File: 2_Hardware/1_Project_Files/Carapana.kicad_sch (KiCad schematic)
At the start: 0 parts

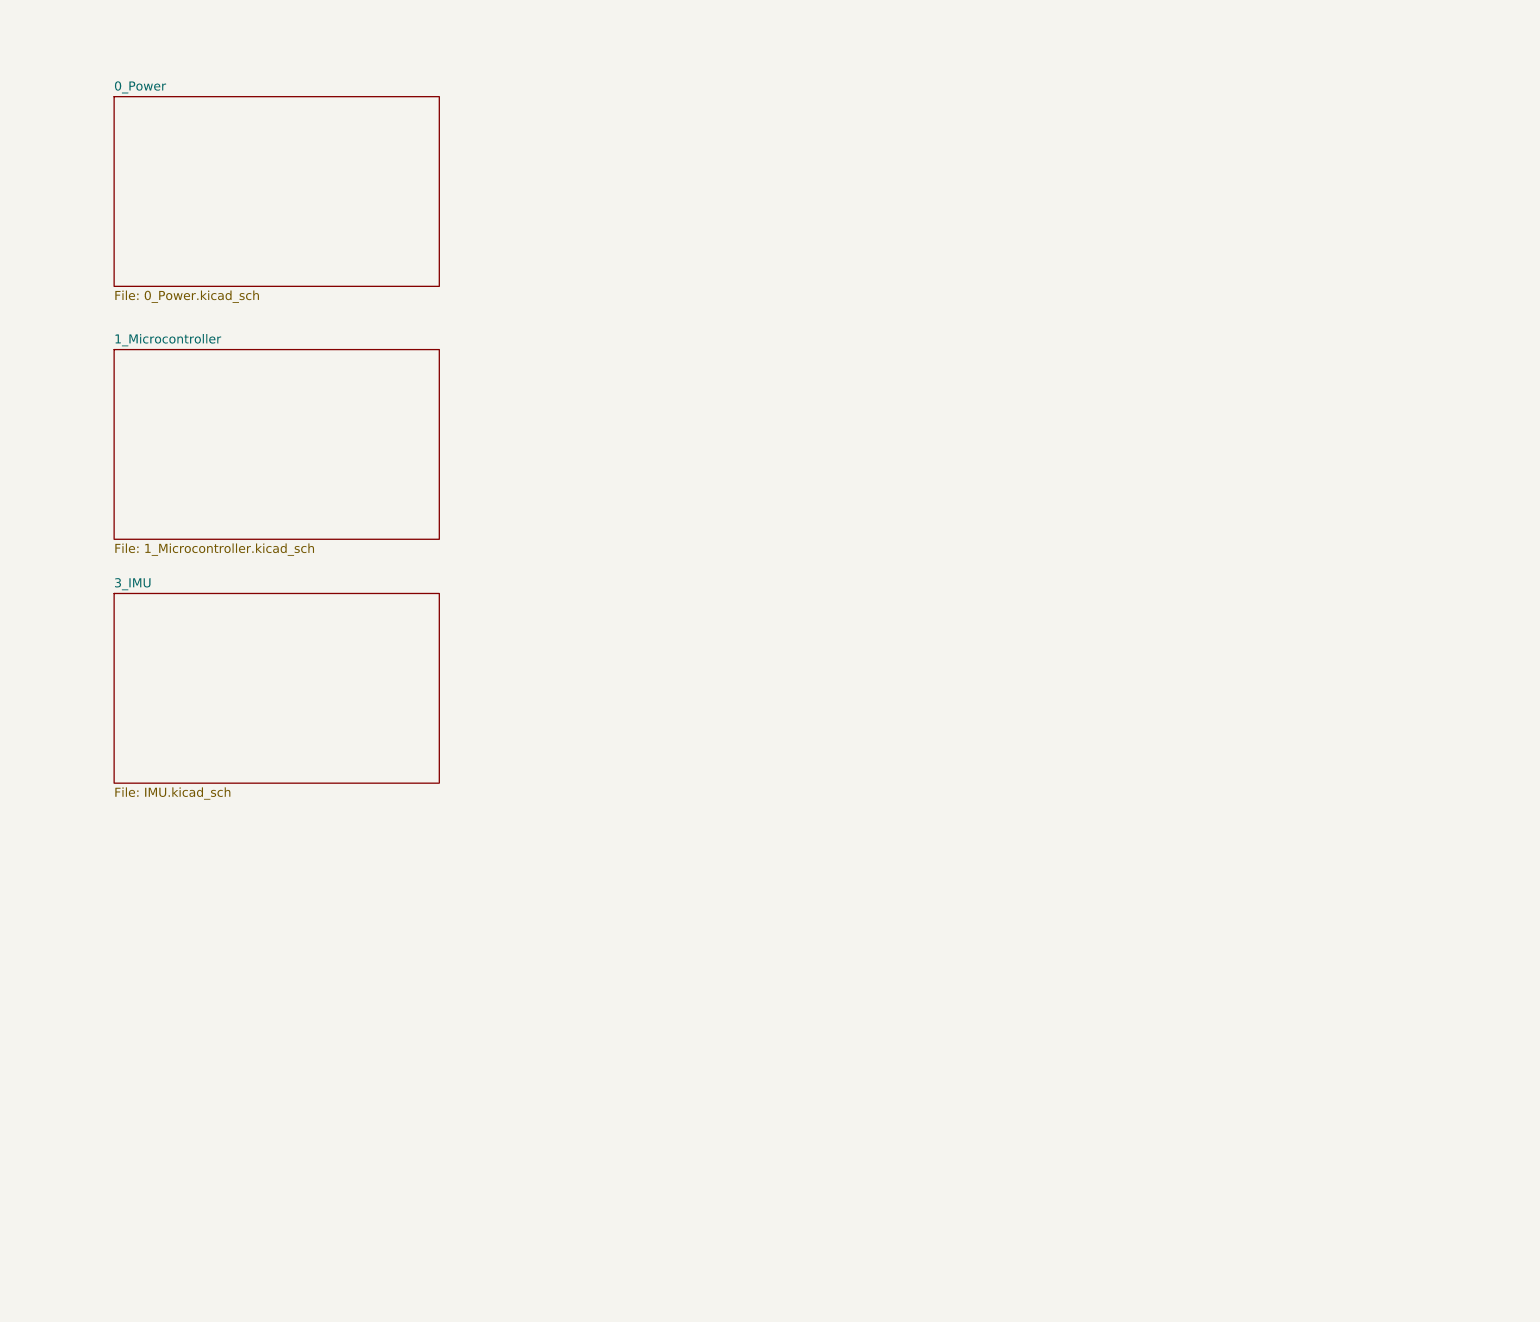
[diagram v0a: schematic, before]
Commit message: Adds 2_Motors schematic sheet and updates block diagram
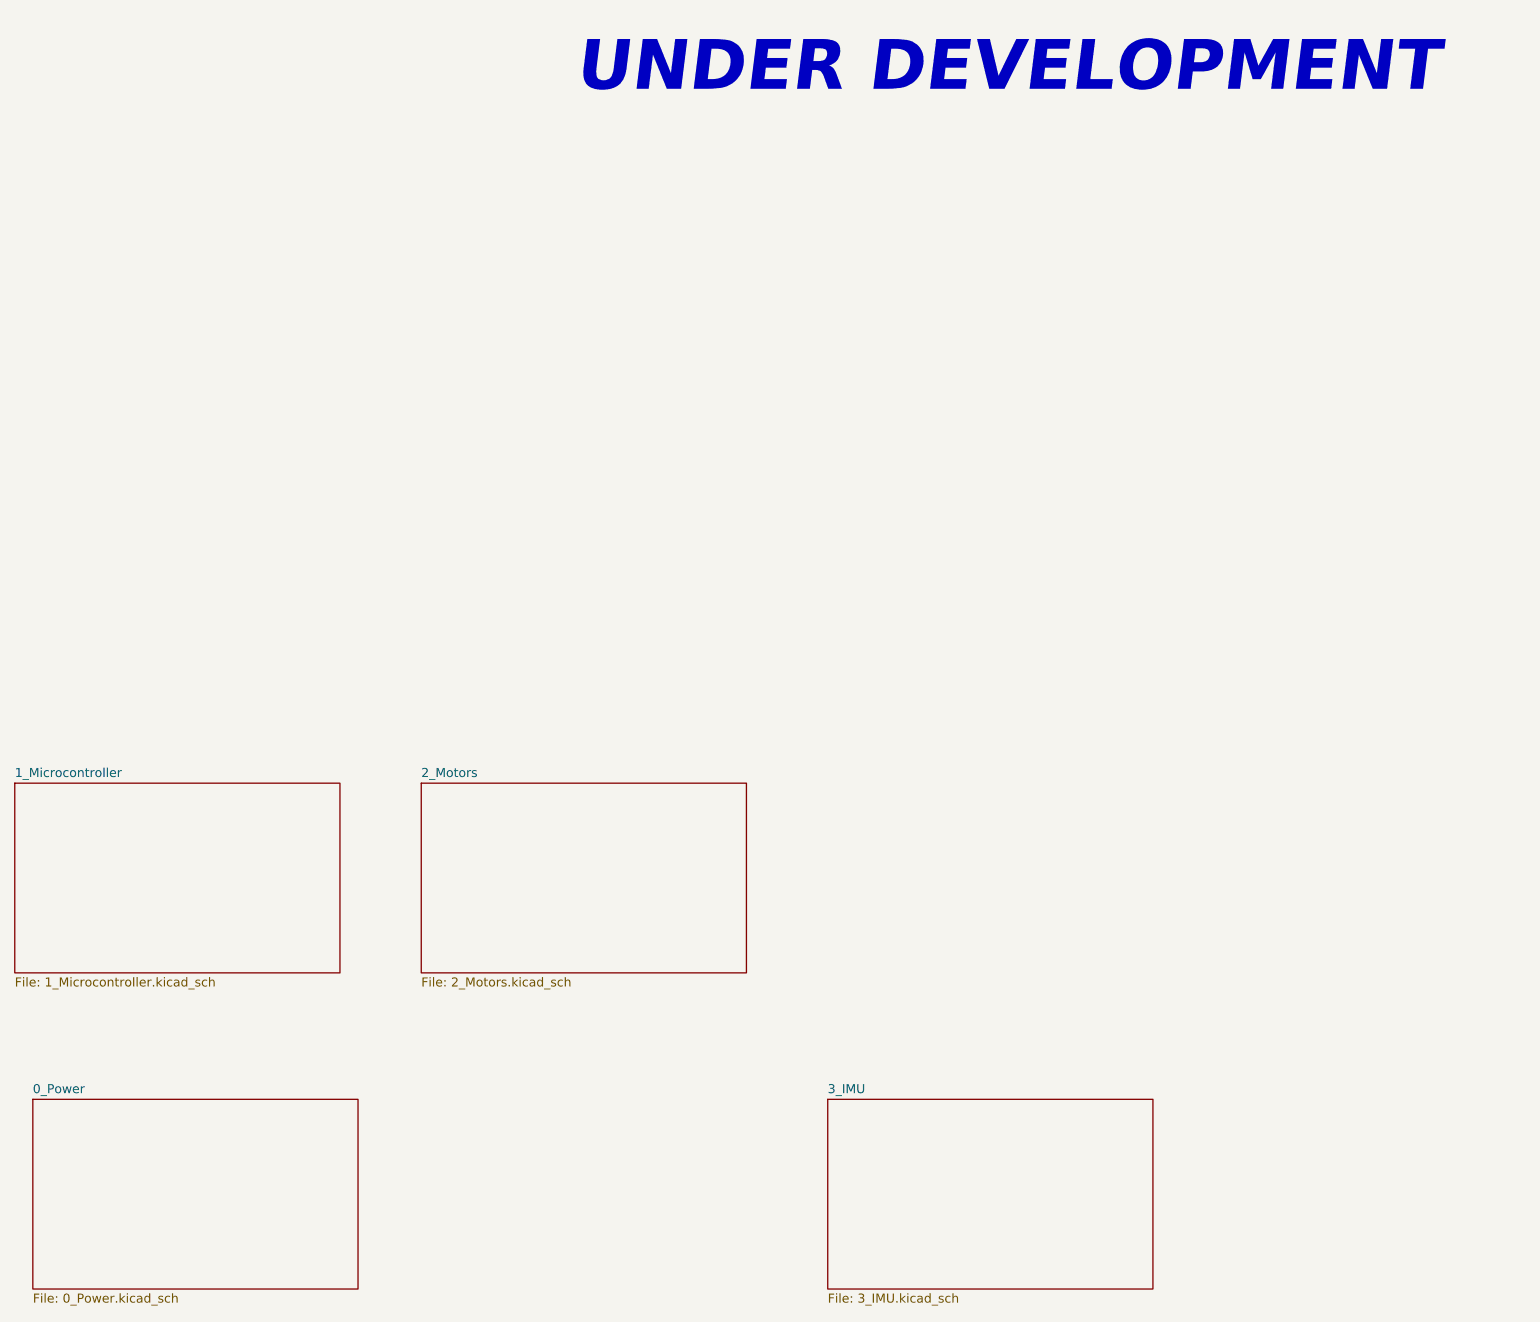
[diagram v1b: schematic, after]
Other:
- added sheet 2_Motors (2_Motors.kicad_sch)
- sheet 3_IMU: file IMU.kicad_sch -> 3_IMU.kicad_sch
- note added: "UNDER DEVELOPMENT"
